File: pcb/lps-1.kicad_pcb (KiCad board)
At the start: 4 copper layers, 66.2 x 30 mm, 26 parts, among them J15 PWR, J4 A_INA219, J5 XBEE, J6 DEV, U1 L7805, U2 ATMega1608_32, U3 TC1262-33

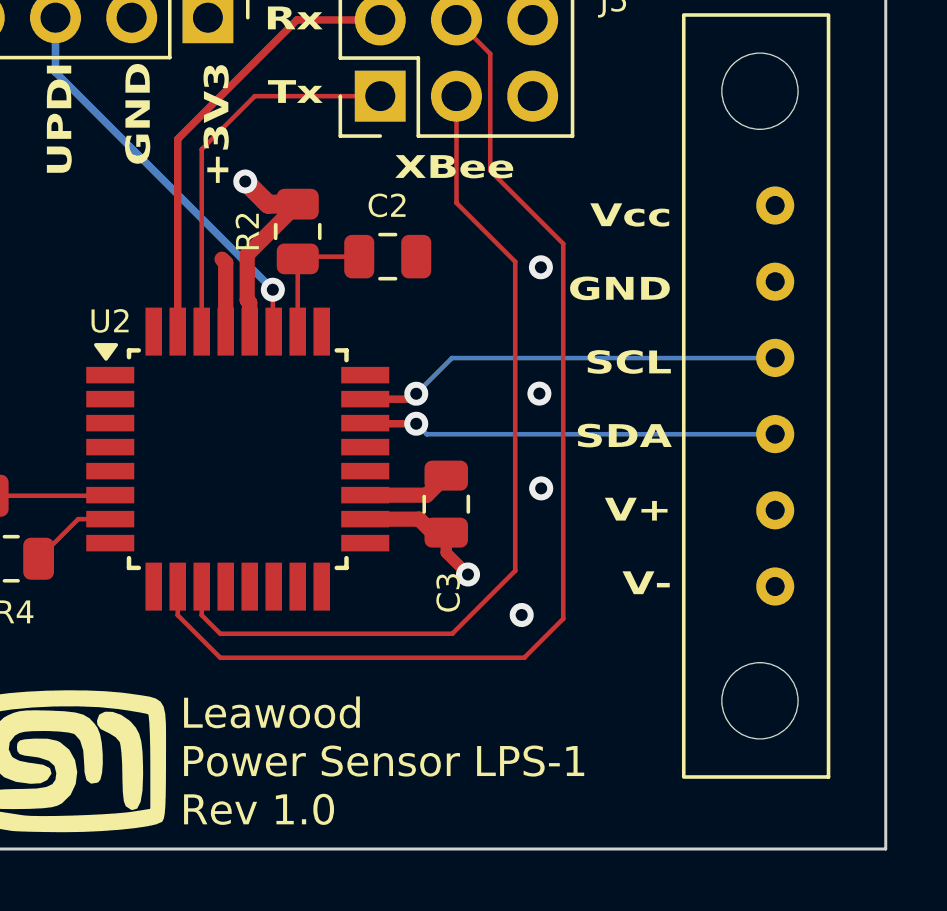
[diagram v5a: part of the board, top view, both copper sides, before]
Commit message: Fixes the drill holes for the INA219
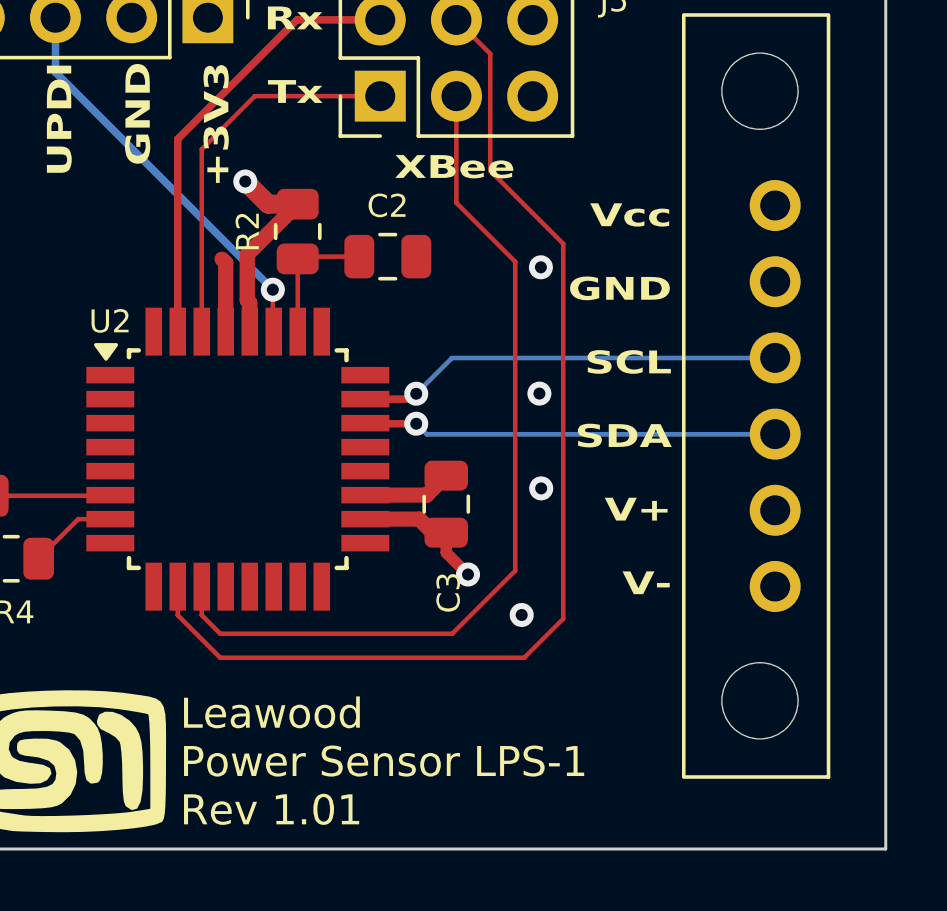
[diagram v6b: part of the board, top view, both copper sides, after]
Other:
- board text added: "Leawood Power Sensor LPS-1 Rev 1.01"
- board text removed: "Leawood Power Sensor LPS-1 Rev 1.0"
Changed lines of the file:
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@@
 	)
 	(paper "A4")
+	(title_block
+		(title "Leawood Power Sensor LPS-1")
+		(date "2024-04-25")
+		(rev "1.01")
+	)
 	(layers
 		(0 "F.Cu" signal)
@@
 			(outputformat 1)
 			(mirror no)
-			(drillshape 1)
+			(drillshape 0)
 			(scaleselection 1)
-			(outputdirectory "")
+			(outputdirectory "lps-1-Gerber/")
 		)
 	)
@@
 			)
 		)
-		(property ki_fp_filters "Connector*:*_1x??_*")
-		(sheetname "Root")
-		(sheetfile "lps-1.kicad_sch")
 		(attr through_hole)
 		(fp_rect
@@
 		(pad "1" thru_hole circle
 			(at -0.016 0 180)
-			(size 1.27 1.27)
-			(drill 0.635)
+			(size 1.7 1.7)
+			(drill 1)
 			(layers "*.Cu" "*.Mask")
 			(remove_unused_layers no)
@@
 		(pad "2" thru_hole circle
 			(at -0.016 -2.54 180)
-			(size 1.27 1.27)
-			(drill 0.635)
+			(size 1.7 1.7)
+			(drill 1)
 			(layers "*.Cu" "*.Mask")
 			(remove_unused_layers no)
@@
 		(pad "3" thru_hole circle
 			(at -0.016 -5.08 180)
-			(size 1.27 1.27)
-			(drill 0.635)
+			(size 1.7 1.7)
+			(drill 1)
 			(layers "*.Cu" "*.Mask")
 			(remove_unused_layers no)
@@
 		(pad "4" thru_hole circle
 			(at -0.016 -7.62 180)
-			(size 1.27 1.27)
-			(drill 0.635)
+			(size 1.7 1.7)
+			(drill 1)
 			(layers "*.Cu" "*.Mask")
 			(remove_unused_layers no)
@@
 		(pad "5" thru_hole circle
 			(at -0.016 -10.16 180)
-			(size 1.27 1.27)
-			(drill 0.635)
+			(size 1.7 1.7)
+			(drill 1)
 			(layers "*.Cu" "*.Mask")
 			(remove_unused_layers no)
@@
 		(pad "6" thru_hole circle
 			(at -0.016 -12.7 180)
-			(size 1.27 1.27)
-			(drill 0.635)
+			(size 1.7 1.7)
+			(drill 1)
 			(layers "*.Cu" "*.Mask")
 			(remove_unused_layers no)
@@
 			(at 0 3.7 0)
 			(layer "F.Fab")
+			(hide yes)
 			(effects
 				(font
@@
 			(at 0 2.6 0)
 			(layer "F.Fab")
+			(hide yes)
 			(effects
 				(font
@@
 			(at 0 3.7 0)
 			(layer "F.Fab")
+			(hide yes)
 			(effects
 				(font
@@
 		(layer "User.1")
 	)
-	(gr_text "Leawood Power Sensor LPS-1\nRev 1.0"
+	(gr_text "Leawood Power Sensor LPS-1\nRev 1.01"
 		(at 118.831 77.159 0)
 		(layer "B.SilkS")
@@
 		)
 	)
-	(gr_text "Leawood \nPower Sensor LPS-1\nRev 1.0"
+	(gr_text "Leawood \nPower Sensor LPS-1\nRev 1.01"
 		(at 105.7 84.3 0)
 		(layer "F.SilkS")
@@
 		)
 		(height -8.36)
-		(gr_text "2.6063 in"
+		(gr_text "66.2000 mm"
 			(at 96.1 45.49 0)
 			(layer "User.1")
@@
 		)
 		(height -15.96)
-		(gr_text "3.4543 in"
+		(gr_text "87.7400 mm"
 			(at 98.94 37.87 0)
 			(layer "User.1")
@@
 		)
 		(height -14.58)
-		(gr_text "3.9370 in"
+		(gr_text "100.0000 mm"
 			(at 100 34.27 0)
 			(layer "User.1")
@@
 		)
 		(height -12.184126)
-		(gr_text "3.1429 in"
+		(gr_text "79.8300 mm"
 			(at 102.918341 41.675874 359.9856456)
 			(layer "User.1")
@@
 		)
 		(height -16.875)
-		(gr_text "1.1811 in"
+		(gr_text "30.0000 mm"
 			(at 144.95 70 90)
 			(layer "User.1")

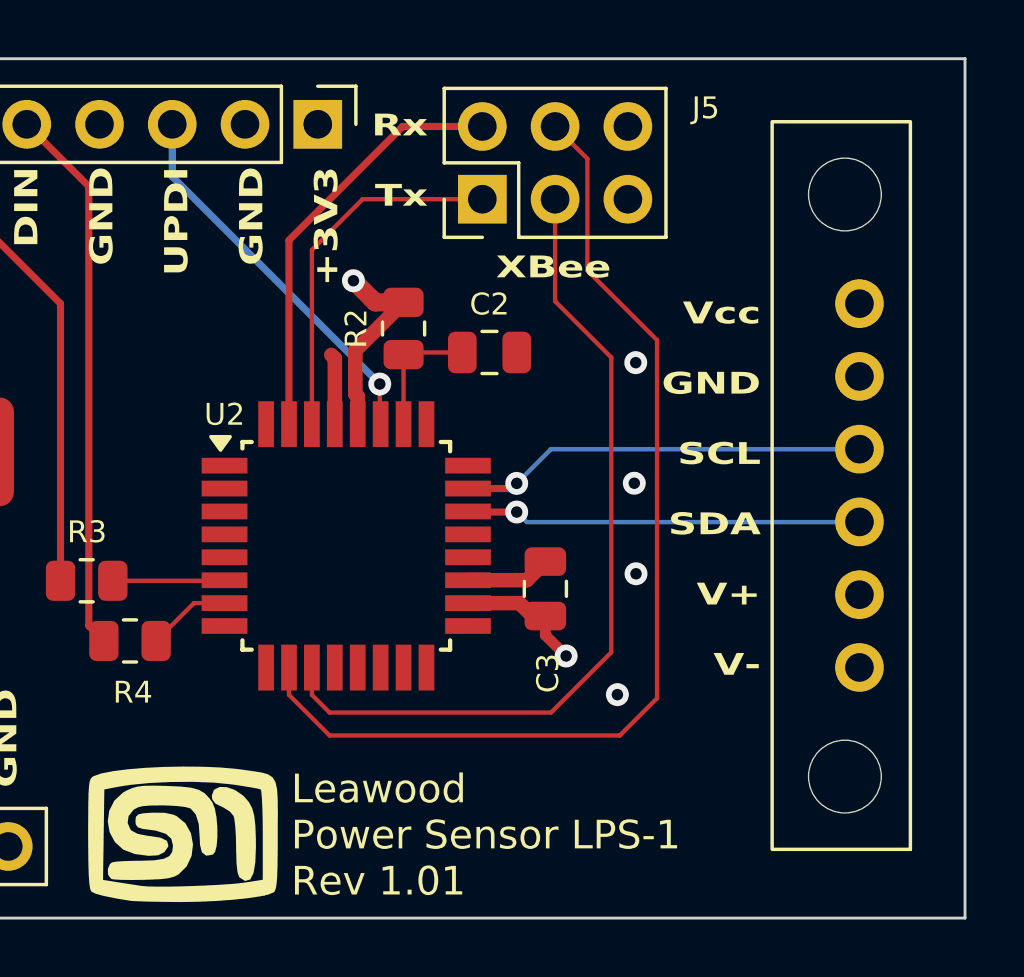
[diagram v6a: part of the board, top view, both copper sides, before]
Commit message: Correction to the TWI0 pin selection
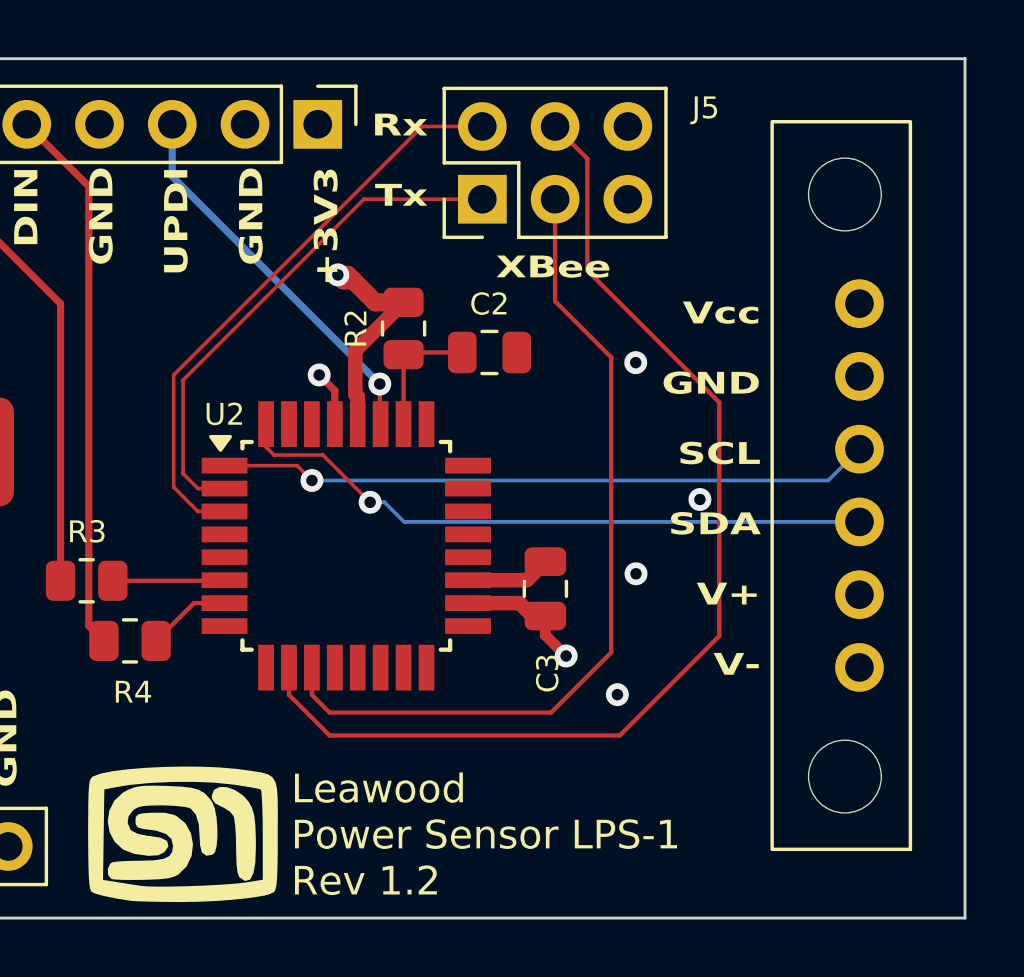
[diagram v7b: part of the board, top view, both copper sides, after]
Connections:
- U2 pad 1: /PA3 -> /SCL
- U2 pad 2: /MOSI -> /TxD0
- U2 pad 22: /SDA -> /PF2
- U2 pad 23: /SCL -> /PF3
- U2 pad 3: /MISO -> /RxD0
- U2 pad 30: /TxD0 -> /PA0
- U2 pad 31: /RxD0 -> /PA1
- U2 pad 32: /PA2 -> /SDA
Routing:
- net /SDA: track 13.8 -> 22.6 mm
- net /SCL: track 14.2 -> 22.8 mm
- net /RxD0: track 14.8 -> 20.4 mm
- net /TxD0: track 12.8 -> 18.0 mm
- net /MODEM_RESET: track 36.4 -> 38.2 mm
- net +3.3V: track 20.1 -> 21.3 mm
- net GND: track 17.0 -> 16.5 mm, vias 4 -> 5
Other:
- board text added: "Leawood Power Sensor LPS-1 Rev 1.2"
- board text removed: "Leawood Power Sensor LPS-1 Rev 1.01"

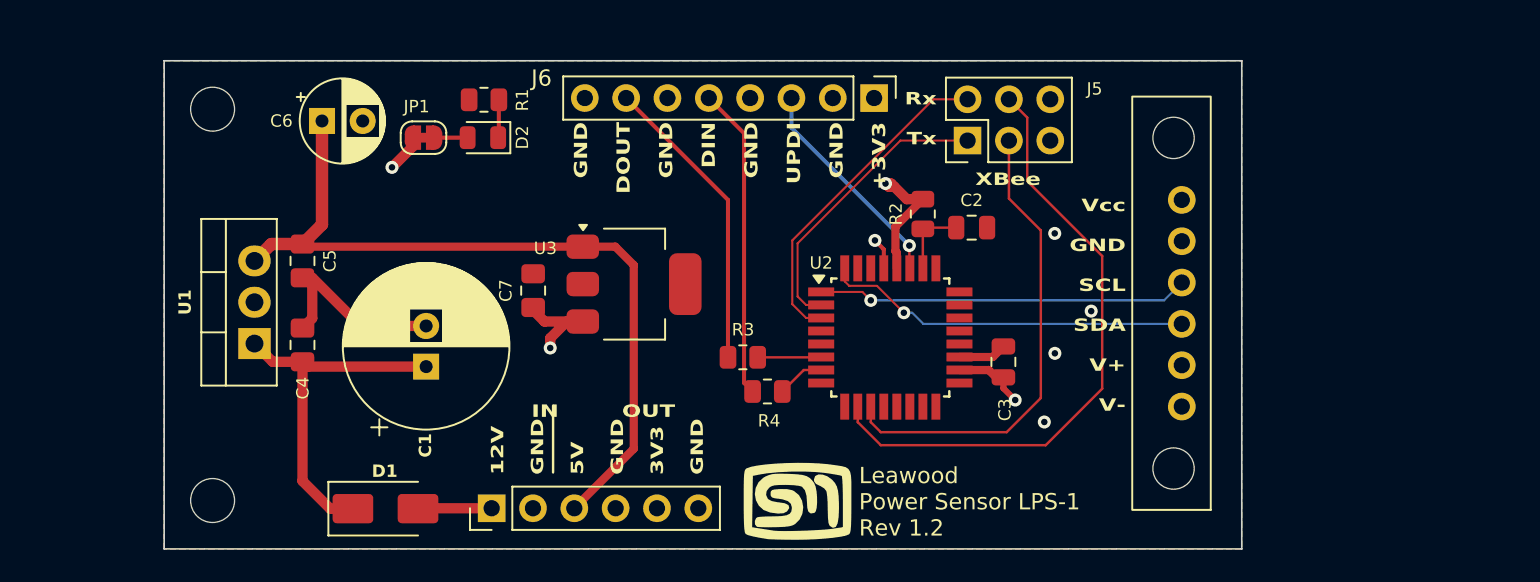
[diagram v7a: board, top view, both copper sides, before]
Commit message: Created keep out zones around the mounting holes
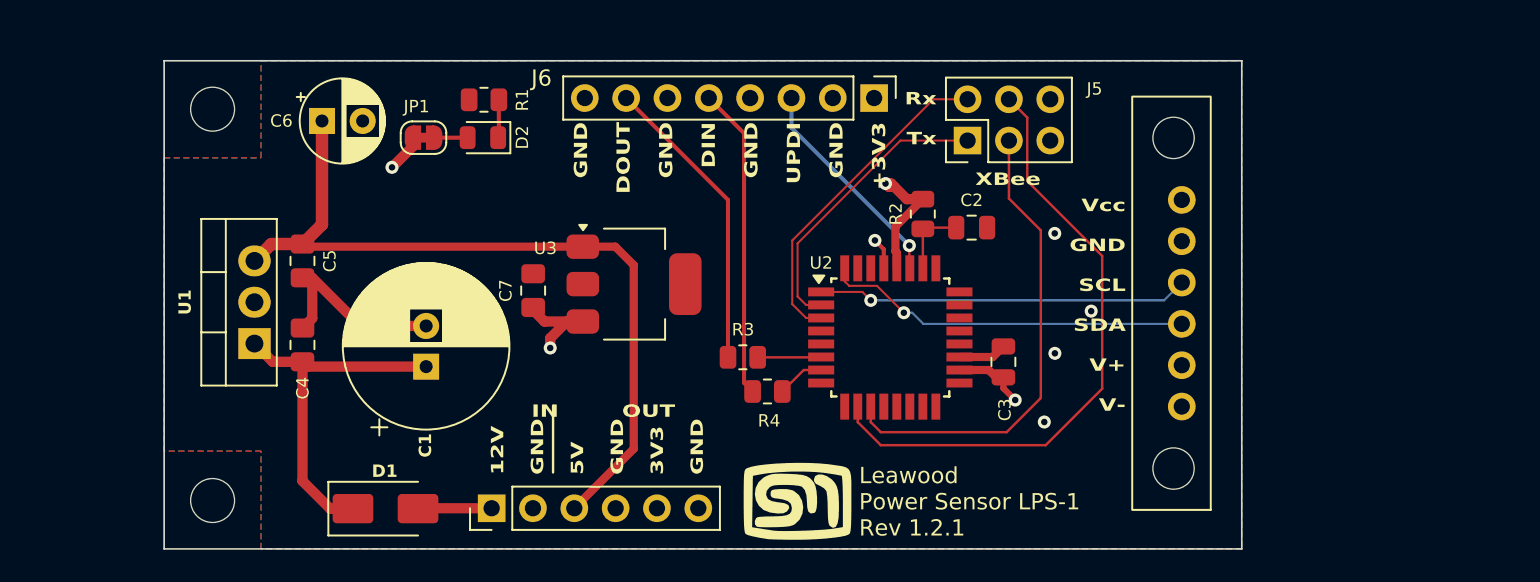
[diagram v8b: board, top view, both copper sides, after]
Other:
- board text added: "Leawood Power Sensor LPS-1 Rev 1.2.1"
- board text removed: "Leawood Power Sensor LPS-1 Rev 1.2"
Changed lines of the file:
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@@
 	(title_block
 		(title "Leawood Power Sensor LPS-1")
-		(date "2024-04-25")
-		(rev "1.2")
+		(date "2024-05-15")
+		(rev "1.2.1")
 	)
 	(layers
@@
 		(layer "User.1")
 	)
-	(gr_text "Leawood Power Sensor LPS-1\nRev 1.2\n"
+	(gr_text "Leawood Power Sensor LPS-1\nRev 1.2.1\n"
 		(at 118.831 77.159 0)
 		(layer "B.SilkS")
@@
 		)
 	)
-	(gr_text "Leawood \nPower Sensor LPS-1\nRev 1.2"
+	(gr_text "Leawood \nPower Sensor LPS-1\nRev 1.2.1\n"
 		(at 105.7 84.3 0)
 		(layer "F.SilkS")
@@
 		)
 		(height -8.36)
-		(gr_text "2606.2992 mils"
+		(gr_text "66.2000 mm"
 			(at 96.1 45.49 0)
 			(layer "User.1")
@@
 		)
 		(height -15.96)
-		(gr_text "3454.3307 mils"
+		(gr_text "87.7400 mm"
 			(at 98.94 37.87 0)
 			(layer "User.1")
@@
 		)
 		(height -14.58)
-		(gr_text "3937.0079 mils"
+		(gr_text "100.0000 mm"
 			(at 100 34.27 0)
 			(layer "User.1")
@@
 		)
 		(height -12.184126)
-		(gr_text "3142.9135 mils"
+		(gr_text "79.8300 mm"
 			(at 102.918341 41.675874 359.9856456)
 			(layer "User.1")
@@
 		)
 		(height -16.875)
-		(gr_text "1181.1024 mils"
+		(gr_text "30.0000 mm"
 			(at 144.95 70 90)
 			(layer "User.1")
@@
 	)
 	(zone
+		(net 0)
+		(net_name "")
+		(layers "F.Cu" "In1.Cu" "In2.Cu" "B.Cu")
+		(hatch edge 0.5)
+		(connect_pads
+			(clearance 0)
+		)
+		(min_thickness 0.25)
+		(filled_areas_thickness no)
+		(keepout
+			(tracks allowed)
+			(vias allowed)
+			(pads allowed)
+			(copperpour not_allowed)
+			(footprints allowed)
+		)
+		(fill
+			(thermal_gap 0.5)
+			(thermal_bridge_width 0.5)
+		)
+		(polygon
+			(pts
+				(xy 122.809 57.658) (xy 127.127 57.658) (xy 127.127 61.849) (xy 122.809 61.849)
+			)
+		)
+	)
+	(zone
+		(net 0)
+		(net_name "")
+		(layers "F.Cu" "In1.Cu" "In2.Cu" "B.Cu")
+		(hatch edge 0.5)
+		(connect_pads
+			(clearance 0)
+		)
+		(min_thickness 0.25)
+		(filled_areas_thickness no)
+		(keepout
+			(tracks allowed)
+			(vias allowed)
+			(pads allowed)
+			(copperpour not_allowed)
+			(footprints allowed)
+		)
+		(fill
+			(thermal_gap 0.5)
+			(thermal_bridge_width 0.5)
+		)
+		(polygon
+			(pts
+				(xy 123.063 77.978) (xy 127.127 77.978) (xy 127.127 82.169) (xy 123.063 82.169)
+			)
+		)
+	)
+	(zone
 		(net 2)
 		(net_name "GND")
@@
 		(polygon
 			(pts
-				(xy 63 55) (xy 129.225 55) (xy 129.225 85) (xy 63 85)
+				(xy 63 78.994) (xy 63 60.96) (xy 68.961 60.96) (xy 68.961 55) (xy 129.225 55) (xy 129.225 85) (xy 68.961 85)
+				(xy 68.961 78.994)
 			)
 		)
@@
 		(polygon
 			(pts
-				(xy 63 55) (xy 129.225 55) (xy 129.225 85) (xy 63 85)
+				(xy 63 78.994) (xy 63 60.96) (xy 68.961 60.96) (xy 68.961 55) (xy 129.225 55) (xy 129.225 85) (xy 68.961 85)
+				(xy 68.961 78.994)
 			)
 		)
@@
 		(polygon
 			(pts
-				(xy 63 55) (xy 129.225 55) (xy 129.225 85) (xy 63 85)
+				(xy 63 78.994) (xy 63 60.96) (xy 68.961 60.96) (xy 68.961 55) (xy 129.225 55) (xy 129.225 85) (xy 68.961 85)
+				(xy 68.961 78.994)
 			)
 		)
